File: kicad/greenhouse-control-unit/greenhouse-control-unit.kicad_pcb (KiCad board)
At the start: 2 copper layers, 72 parts, among them J1 Pluggable_Terminal_01x02, J10 Molex_KK-254_01x10, J10_LittleBuck1 Conn_01x01_Female, J11_LittleBuck1 Conn_01x01_Female, J12_BigBuck1 Conn_01x01_Female, J13_BigBuck1 Conn_01x01_Female, J14_LittleBuck1 Conn_01x01_Female, J15_LittleBuck1 Conn_01x01_Female, J2 Pluggable_Terminal_01x02, J3 Pluggable_Terminal_01x02, J4 Molex_KK-254_01x08, J5 Conn_01x10_Female, J6 Conn_01x10_Female, J6_BigBuck1 Conn_01x01_Female, J7 Conn_01x15_Female, J7_BigBuck1 Conn_01x01_Female, J8 Conn_01x15_Female, J9 Molex_KK-396_01x16, Q1 2N7000, Q10 IRLB8721PBF, Q11 IRLB8721PBF, Q12 2N7000, Q13 2N7000, Q2 2N7000, Q3 2N7000, Q4 IRLB8721PBF, Q5 IRLB8721PBF, Q6 IRLB8721PBF, Q7 IRLB8721PBF, Q8 IRLB8721PBF, Q9 IRLB8721PBF, U1 74HC595, U2 74HC595

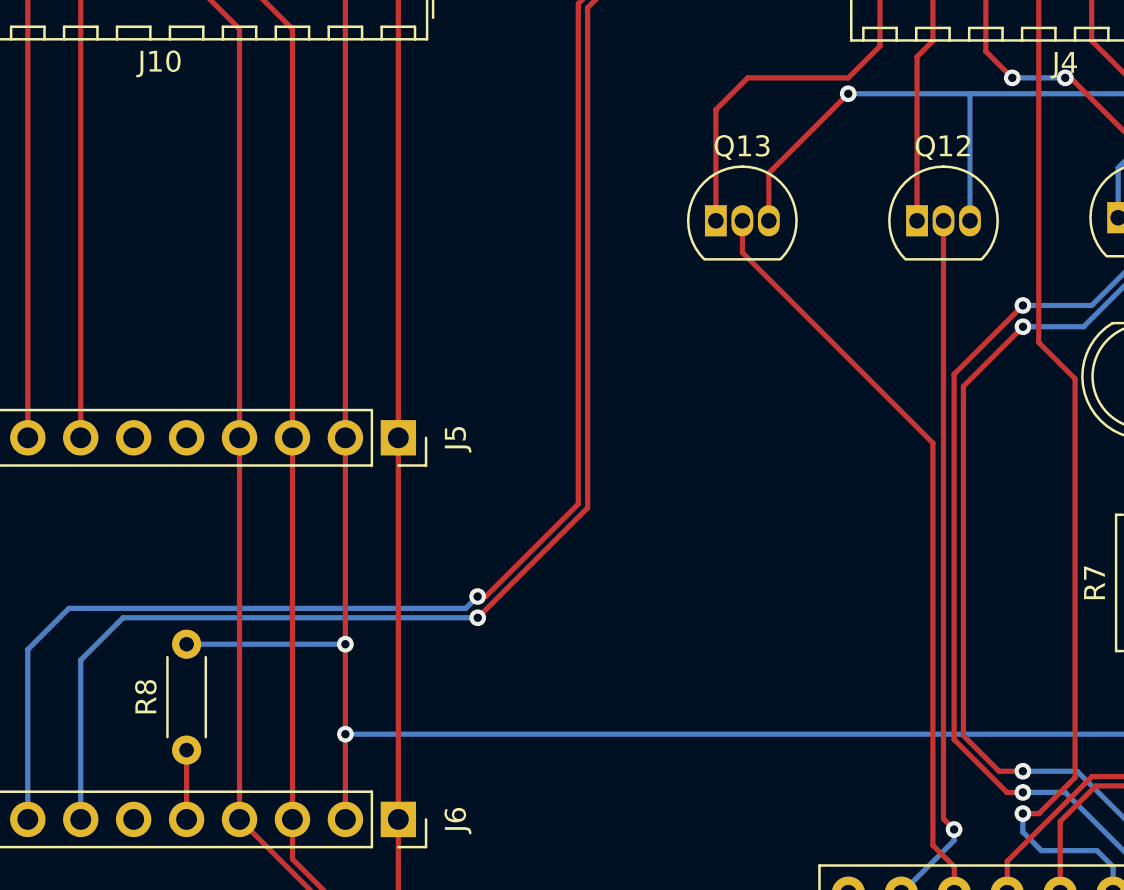
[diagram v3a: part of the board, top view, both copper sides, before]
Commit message: Remove FETs for motor controller; not needed if EN is 5V
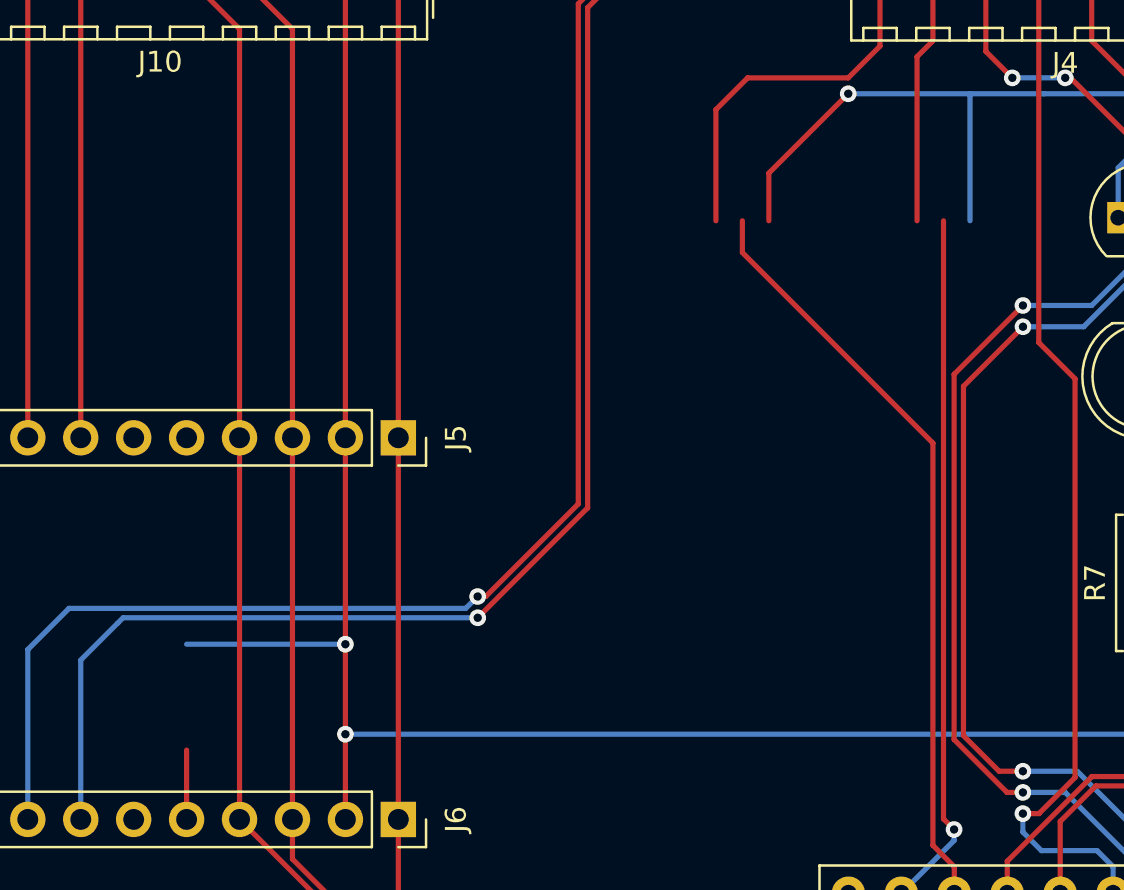
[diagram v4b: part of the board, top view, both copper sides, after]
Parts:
- removed Q12, Q13: 2N7000, Package_TO_SOT_THT:TO-92_Inline
- removed R8: 10k, Resistor_THT:R_Axial_DIN0204_L3.6mm_D1.6mm_P5.08mm_Horizontal
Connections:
- net /SR_VCC renamed /SR_CLR
- J4 pad 7: /Motor_IN2 -> /Motor1_SR_Q6
- J4 pad 8: /Motor_IN1 -> /Motor2_SR_Q7
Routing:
- net /Motor_IN1: track 17.8 -> 0.00 mm
- net /Motor2_SR_Q7: track 33.5 -> 51.3 mm
- net /Motor_IN2: track 12.0 -> 0.00 mm
- net /Motor1_SR_Q6: track 36.5 -> 48.5 mm

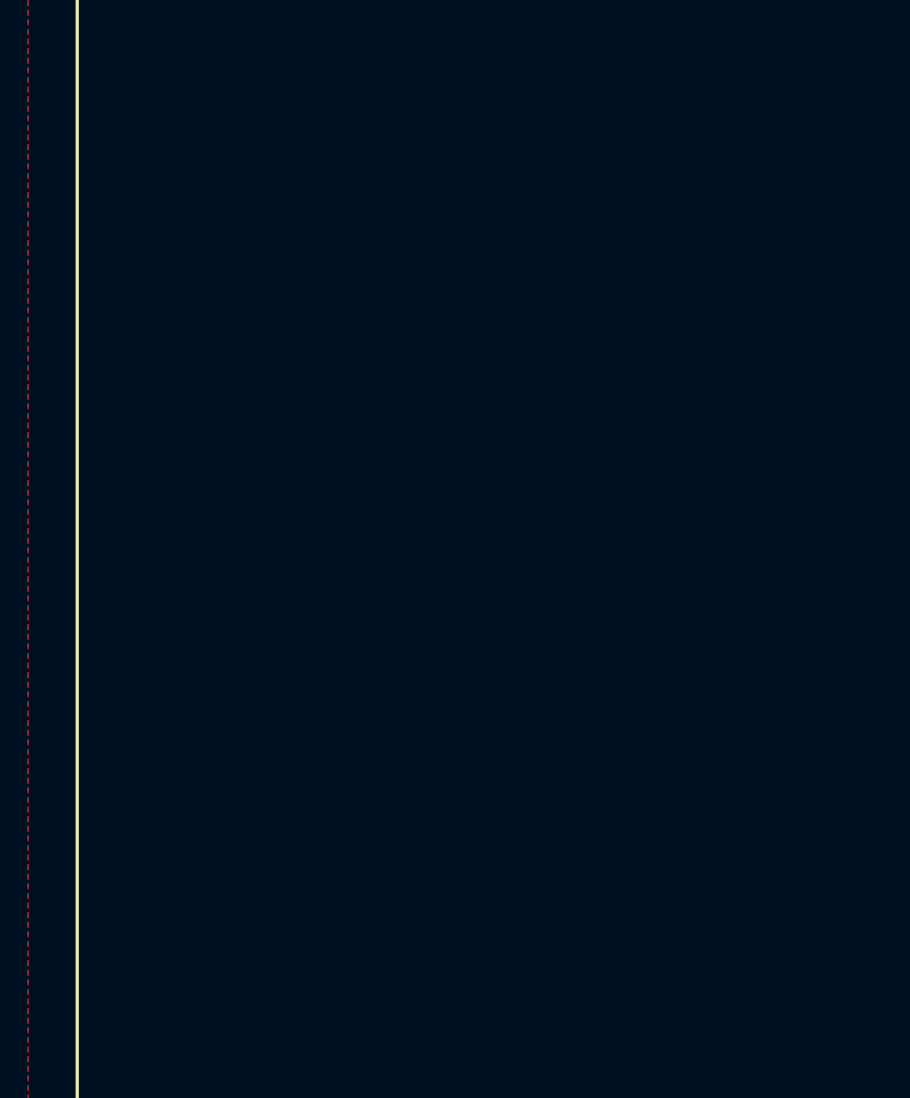
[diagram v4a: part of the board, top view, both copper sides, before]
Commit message: New schematic for L298N motor driver
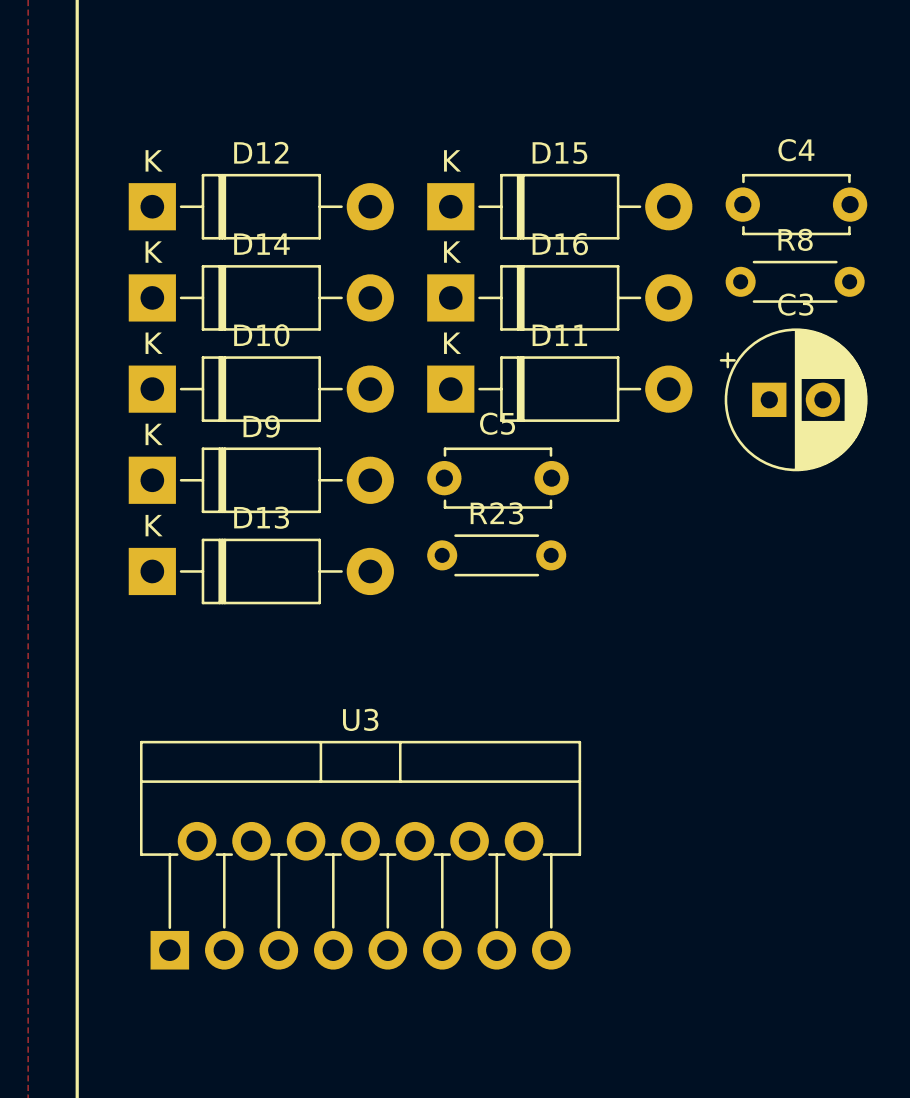
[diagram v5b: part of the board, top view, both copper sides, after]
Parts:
- added C3: 220uF, Capacitor_THT:CP_Radial_D6.3mm_P2.50mm, F.Cu at (287.3, 76.2)
- added C4: 100nF, Capacitor_THT:C_Disc_D4.7mm_W2.5mm_P5.00mm, F.Cu at (286.0, 67.1)
- added C5: 100nF, Capacitor_THT:C_Disc_D4.7mm_W2.5mm_P5.00mm, F.Cu at (272.1, 79.8)
- added D10: 1N4007, Diode_THT:D_DO-41_SOD81_P10.16mm_Horizontal, F.Cu at (258.5, 75.7)
- added D11: 1N4007, Diode_THT:D_DO-41_SOD81_P10.16mm_Horizontal, F.Cu at (272.4, 75.7)
- added D12: 1N4007, Diode_THT:D_DO-41_SOD81_P10.16mm_Horizontal, F.Cu at (258.5, 67.2)
- added D13: 1N4007, Diode_THT:D_DO-41_SOD81_P10.16mm_Horizontal, F.Cu at (258.5, 84.2)
- added D14: 1N4007, Diode_THT:D_DO-41_SOD81_P10.16mm_Horizontal, F.Cu at (258.5, 71.5)
- added D15: 1N4007, Diode_THT:D_DO-41_SOD81_P10.16mm_Horizontal, F.Cu at (272.4, 67.2)
- added D16: 1N4007, Diode_THT:D_DO-41_SOD81_P10.16mm_Horizontal, F.Cu at (272.4, 71.5)
- added D9: 1N4007, Diode_THT:D_DO-41_SOD81_P10.16mm_Horizontal, F.Cu at (258.5, 80.0)
- added R23: 10k, Resistor_THT:R_Axial_DIN0204_L3.6mm_D1.6mm_P5.08mm_Horizontal, F.Cu at (272.0, 83.5)
- added R8: 10k, Resistor_THT:R_Axial_DIN0204_L3.6mm_D1.6mm_P5.08mm_Horizontal, F.Cu at (285.9, 70.7)
- added U3: L298HN, Package_TO_SOT_THT:TO-220-15_P2.54x2.54mm_StaggerOdd_Lead4.58mm_Vertical, F.Cu at (259.3, 101.9)

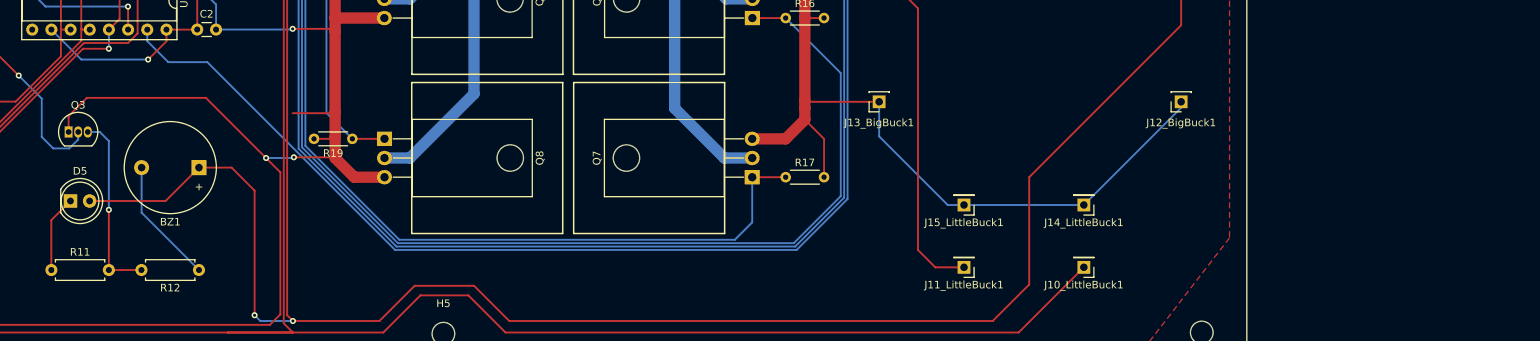
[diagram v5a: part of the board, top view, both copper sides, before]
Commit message: Changed buzzer FET back to BJT
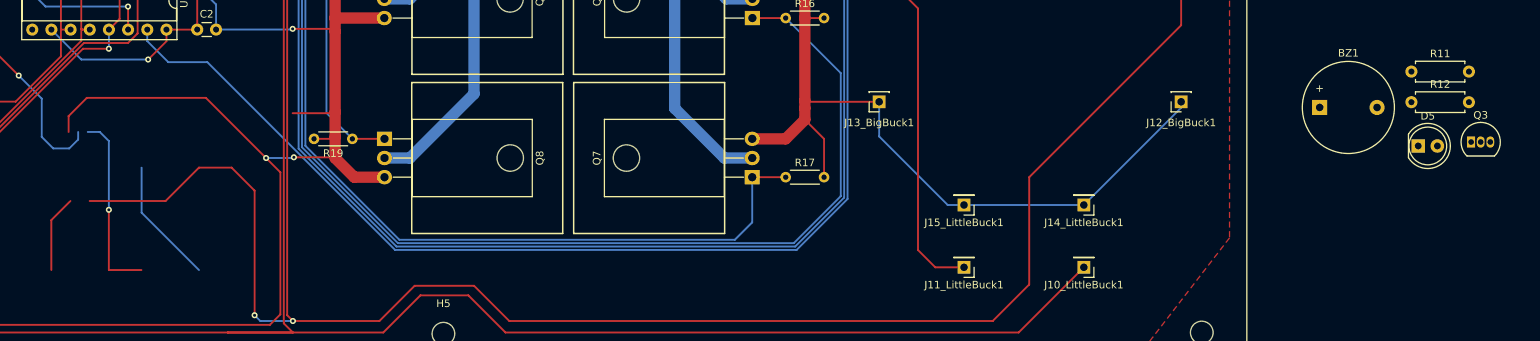
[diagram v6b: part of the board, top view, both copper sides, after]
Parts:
- Q3: value 2N7000 -> 2N2222A
- moved Q3 185.8 mm to (284.7, 125.5)
- moved R11 182.1 mm to (276.8, 116.2)
- moved D5 178.7 mm to (277.7, 126.0)
- moved R12 162.1 mm to (276.8, 120.2), turned to 0 degrees
- moved BZ1 148.7 mm to (264.7, 120.9), turned to 0 degrees
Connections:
- BZ1 pad 1: +5V -> Net-(BZ1-Pad1)
- BZ1 pad 2: Net-(BZ1-Pad2) -> GND
- D5 pad 1: Net-(D5-Pad1) -> GND
- D5 pad 2: +5V -> Net-(D5-Pad2)
- Q3 pad 1: GND -> Net-(Q3-Pad1)
- Q3 pad 3: Net-(Q3-Pad3) -> +5V
- R11 pad 1: Net-(D5-Pad1) -> Net-(Q3-Pad1)
- R11 pad 2: Net-(Q3-Pad3) -> Net-(D5-Pad2)
- R12 pad 1: Net-(BZ1-Pad2) -> Net-(Q3-Pad1)
- R12 pad 2: Net-(Q3-Pad3) -> Net-(BZ1-Pad1)
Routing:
- net (no net): track 0.00 -> 51.6 mm, vias 0 -> 1
- net Net-(Q3-Pad3): track 24.7 -> 0.00 mm, vias 1 -> 0
- net Net-(BZ1-Pad2): track 16.7 -> 0.00 mm
- net Net-(D5-Pad1): track 10.2 -> 0.00 mm

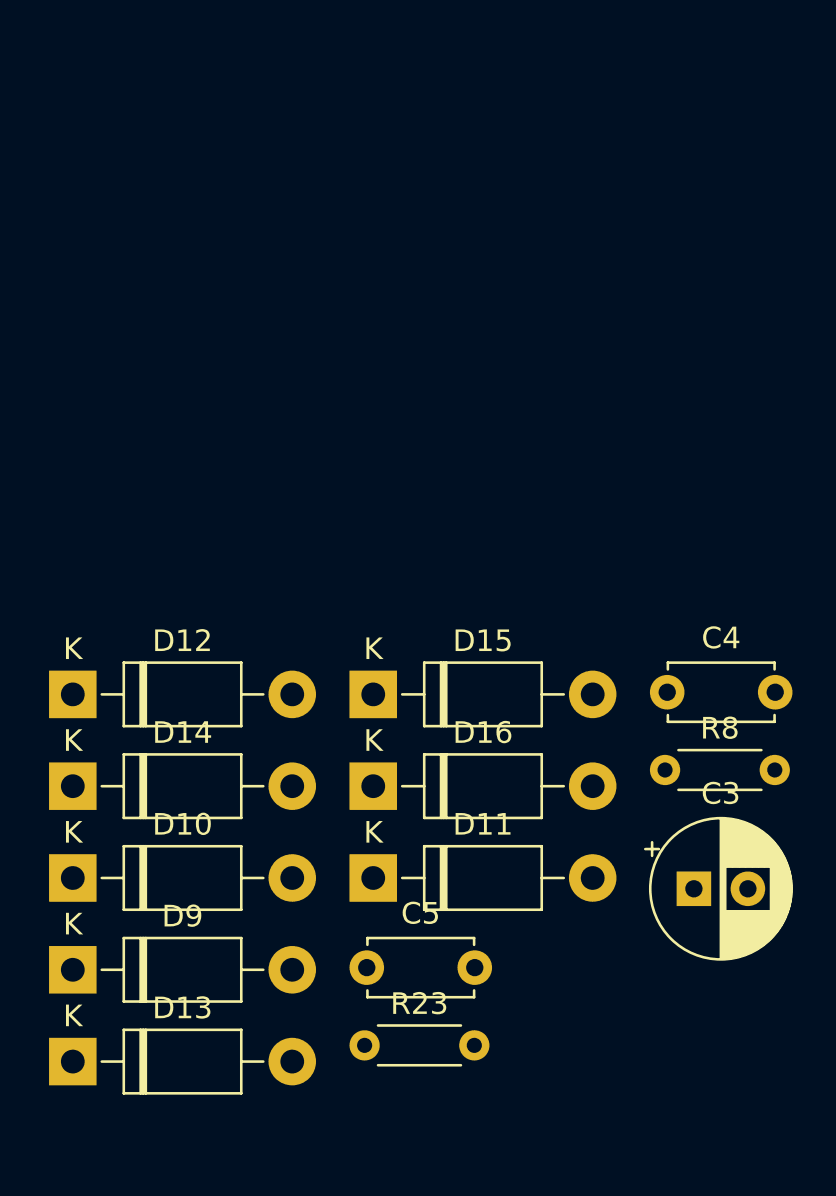
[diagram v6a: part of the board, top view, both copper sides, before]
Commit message: Add voltage regulator to motor driver
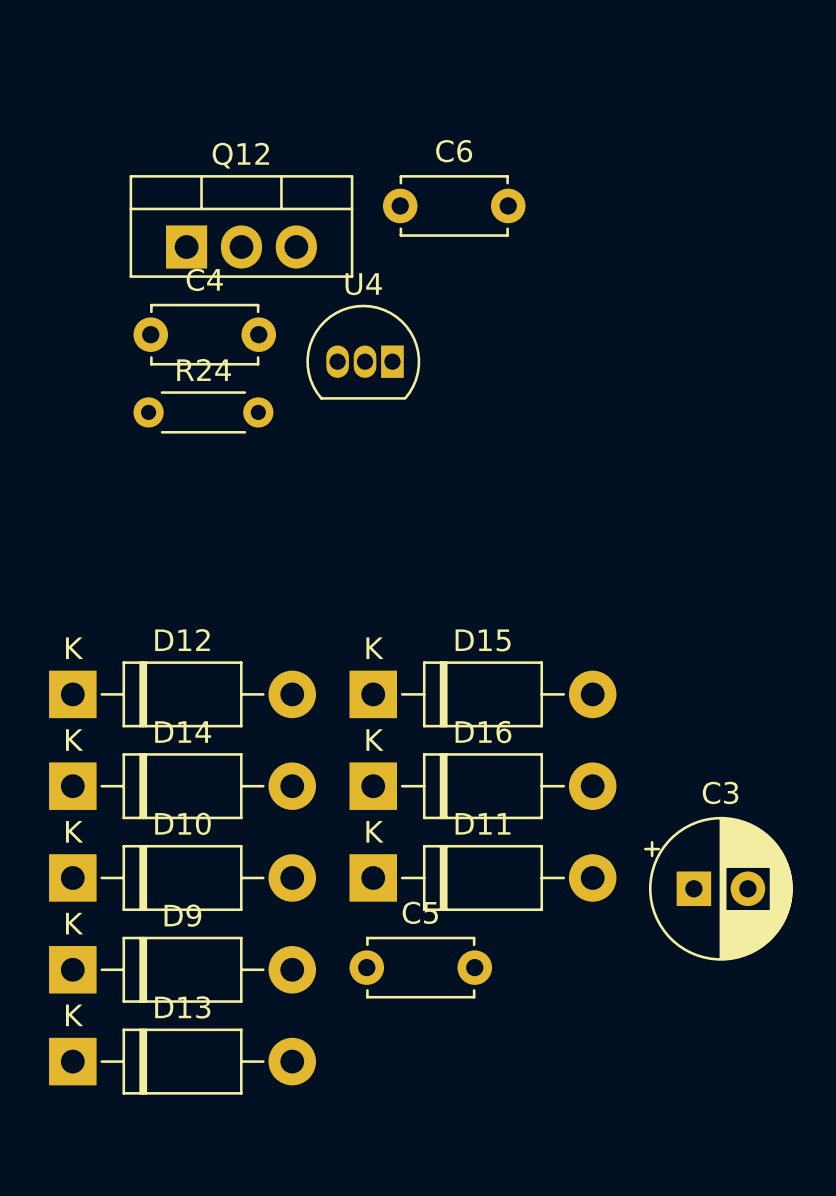
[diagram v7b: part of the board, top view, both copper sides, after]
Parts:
- removed R23, R8: 10k, Resistor_THT:R_Axial_DIN0204_L3.6mm_D1.6mm_P5.08mm_Horizontal
- added C6: 100nF, Capacitor_THT:C_Disc_D4.7mm_W2.5mm_P5.00mm, F.Cu at (273.7, 44.6)
- added Q12: D44H8, Package_TO_SOT_THT:TO-220-3_Vertical, F.Cu at (263.8, 46.5)
- added R24: 100R, Resistor_THT:R_Axial_DIN0204_L3.6mm_D1.6mm_P5.08mm_Horizontal, F.Cu at (262.0, 54.1)
- added U4: WS78L10, Nick:TO-92L_Inline_China, F.Cu at (270.8, 51.8)
- moved C4 29.1 mm to (262.1, 50.5)
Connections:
- C3 pad 1: +12V -> /L298N motor driver/Motor+10V
- C4 pad 1: +12V -> GND
- C4 pad 2: GND -> +12V
- U3 pad 1: Net-(R23-Pad1) -> GND
- U3 pad 11: Net-(R8-Pad2) -> +5V
- U3 pad 15: Net-(R23-Pad1) -> GND
- U3 pad 6: Net-(R8-Pad2) -> +5V
- U3 pad 9: +12V -> /L298N motor driver/Motor+10V
